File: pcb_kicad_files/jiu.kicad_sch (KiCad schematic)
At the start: 173 parts, among them J1 2x3 2.54mm pitch pin header, J2 TYPE-C-31-M-12, J3 1x5 2.54mm pitch pin header, J4 2x9 2.54mm pitch pin header, Q1 DTC123JKAT146, SW1 1U, SW10 1U, SW11 1U, SW12 1U, SW13 1U, SW14 1U, SW15 1U, SW16 2u, SW17 1.5U, SW18 1U, SW19 1U, SW2 1U, SW20 1U, SW21 1U, SW22 1U, SW23 1U, SW24 1U, SW25 1U, SW26 1U, SW27 1U, SW28 1U, SW29 1U, SW3 1U, SW30 1.5U, SW31 1U, SW32 1.75U, SW33 1U, SW34 1U, SW35 1U, SW36 1U, SW37 1U, SW38 1U, SW39 1U, SW4 1U, SW40 1U, SW41 1U, SW42 1U, SW43 1U, SW44 2.25U, SW45 1U, SW46 1.25U, SW47 2.25U, SW48 1U, SW49 1U, SW5 1U, SW50 1U, SW51 1U, SW52 1U, SW53 1U, SW54 1U, SW55 1U, SW56 1U, SW57 1U, SW58 1.75U, SW59 1U, SW6 1U, SW60 1U, SW61 1.5U, SW62 1U, SW63 1.5U, SW64 7U, SW65 1.5U, SW66 1U, SW67 1U, SW68 1U, SW69 1.25U, SW7 1U, SW70 1.25U, SW71 1.25U, SW72 6.25U, SW73 1.25U, SW74 K2-1187SQ-A4SW-06, SW8 1U, SW9 1U, U1 USBLC6-2SC6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

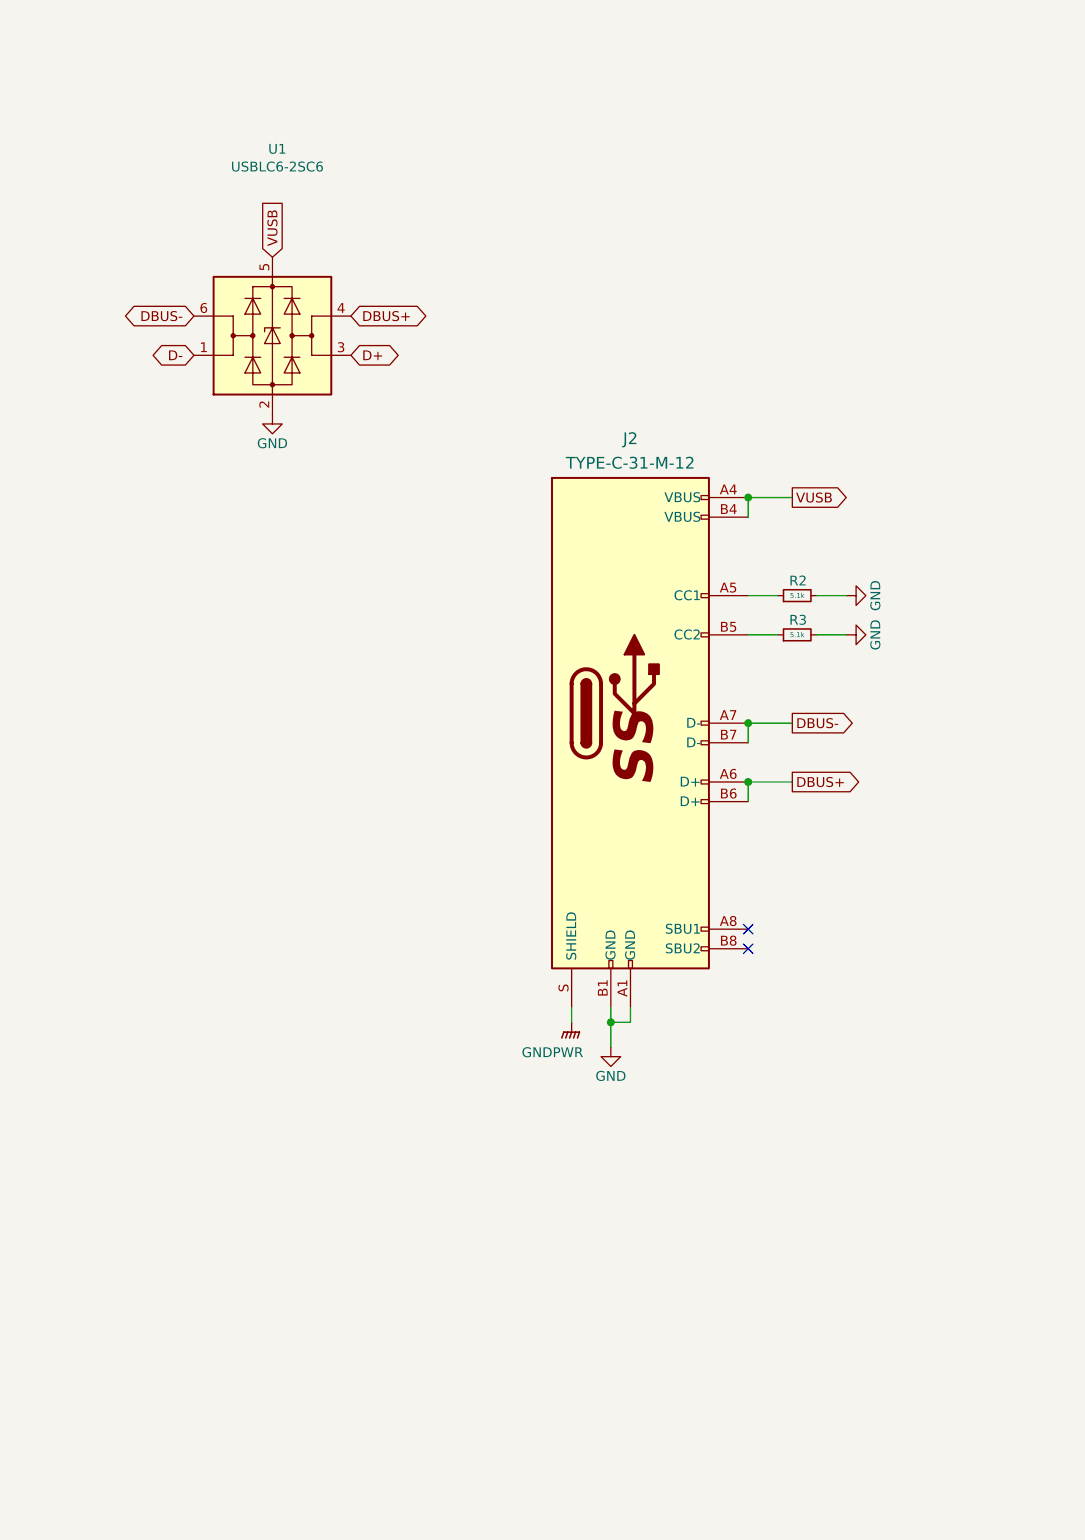
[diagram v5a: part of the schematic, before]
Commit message: Added ferrite bead to USB shield and ground
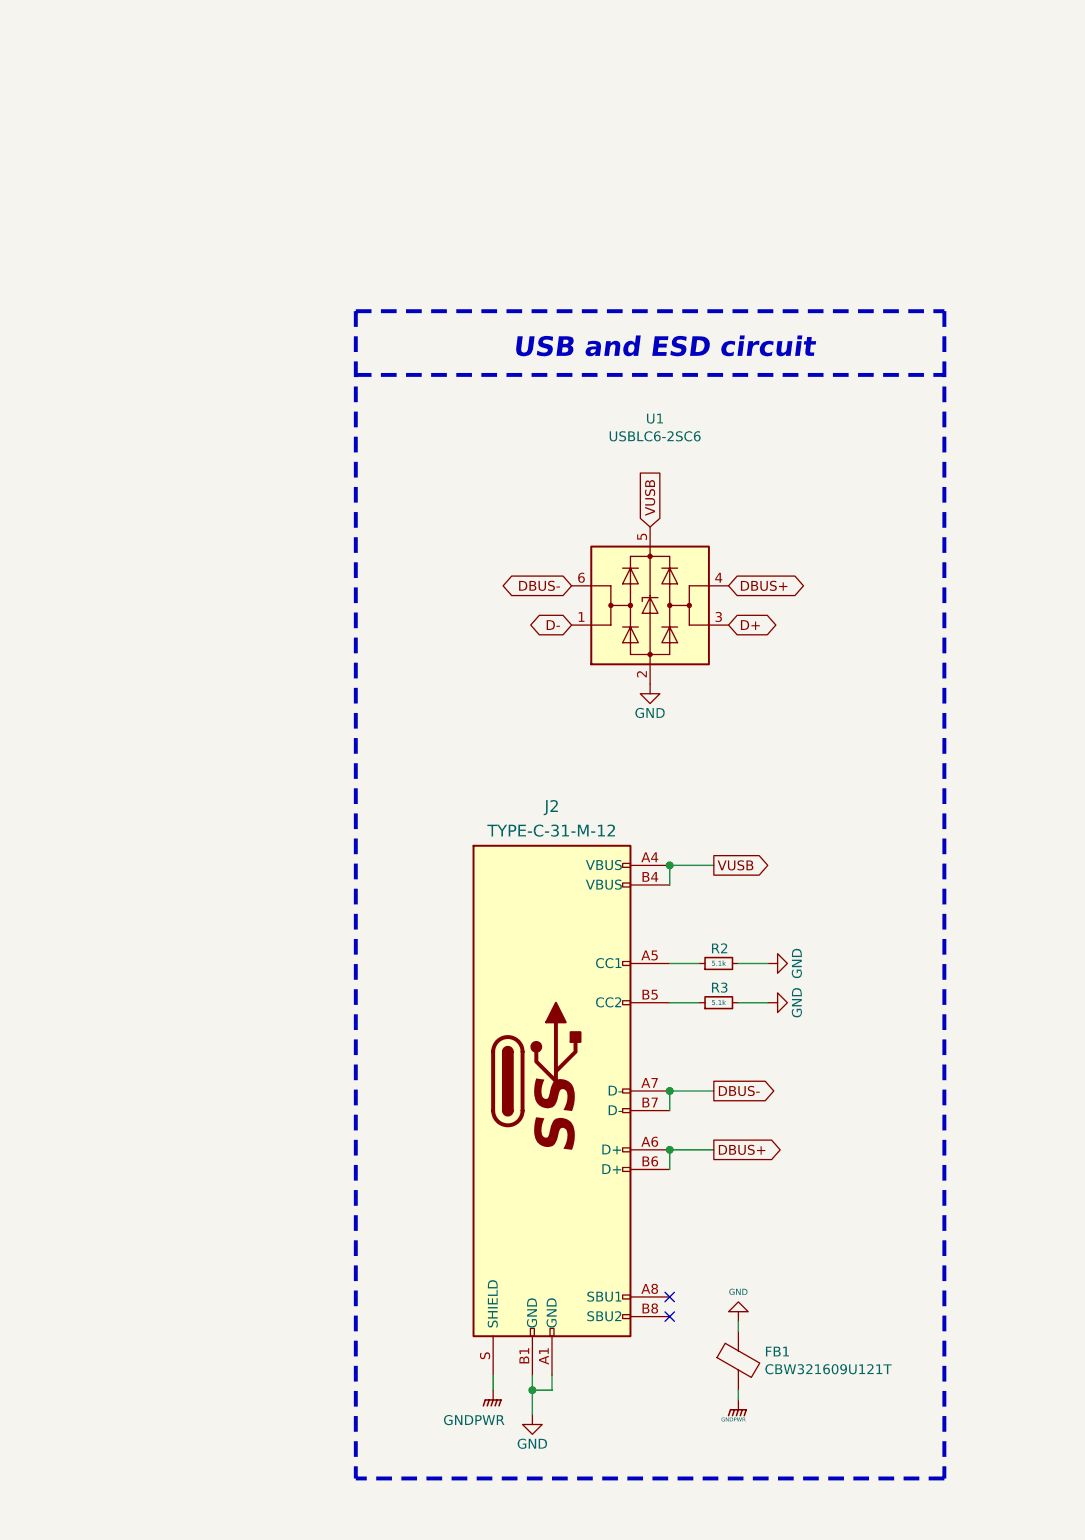
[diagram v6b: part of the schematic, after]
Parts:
- added FB1: CBW321609U121T, Inductor_SMD:L_1206_3216Metric, symbol Device:Ferrite_Bead
- D67: Package (none) -> SOD-123
- D68: Manufacturer (none) -> ROHM Semicon; Manufacturer Part Number (none) -> RB060M-60TR; Package (none) -> SOD-123; Specification (none) -> Power rectifier schottky diode
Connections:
- net GND: now also FB1.1
- net GNDPWR: now also FB1.2
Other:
- note added: "USB and ESD circuit"
- moved on the sheet: J2, R2, R3, U1

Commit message: Preparing for pre-release Alpha
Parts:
- C1, C4: Package (none) -> C0805; Specification (none) -> MLCC 10V
- C10, C9: Package (none) -> CT3216
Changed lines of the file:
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@@
+      (effects (font (size 1.27 1.27)) hide)
+    )
+    (property "Package" "CT3216" (id 4) (at 195.58 340.995 0)
       (effects (font (size 1.27 1.27)) hide)
     )
@@
       (effects (font (size 1.27 1.27)) hide)
     )
+    (property "Package" "CT3216" (id 4) (at 213.36 340.995 0)
+      (effects (font (size 1.27 1.27)) hide)
+    )
   )
   (symbol (lib_id "Device:C_Small") (at 203.835 261.62 180) (unit 1)
@@
     )
     (property "Datasheet" "~" (id 3) (at 203.835 261.62 0)
+      (effects (font (size 1.27 1.27)) hide)
+    )
+    (property "Package" "C0805" (id 4) (at 203.835 261.62 0)
+      (effects (font (size 1.27 1.27)) hide)
+    )
+    (property "Specification" "MLCC 10V" (id 4) (at 203.835 261.62 0)
       (effects (font (size 1.27 1.27)) hide)
     )
@@
       (effects (font (size 1.27 1.27)) hide)
     )
+    (property "Package" "C0805" (id 4) (at 209.55 285.75 0)
+      (effects (font (size 1.27 1.27)) hide)
+    )
+    (property "Specification" "MLCC 10V" (id 4) (at 209.55 285.75 0)
+      (effects (font (size 1.27 1.27)) hide)
+    )

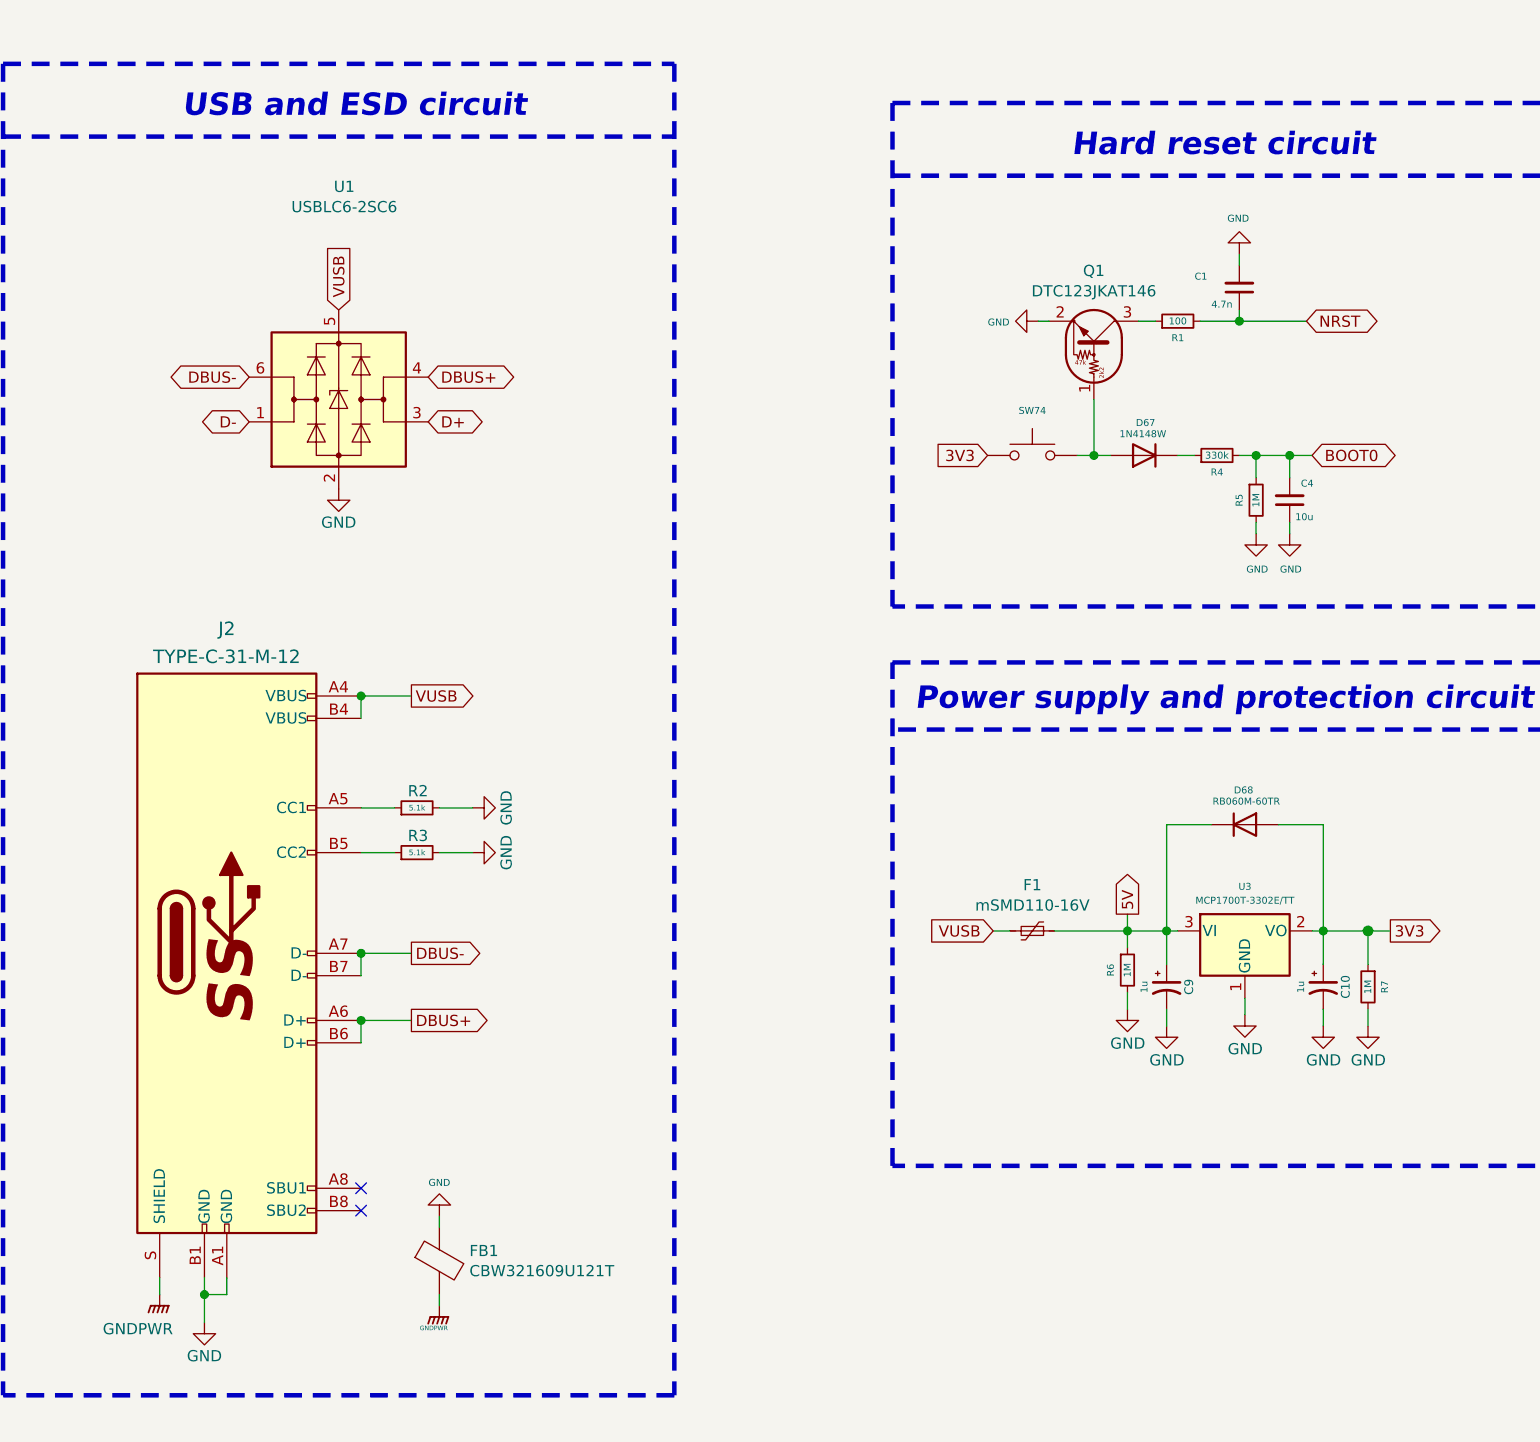
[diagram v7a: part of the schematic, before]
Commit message: Change components and ratings to JLC assembly
- Components were swapped for units that could be soldered in JLCPCB's assembly using the most basic components possible
- All resistors were changed to 0805
- Reset button was removed and instead reset contacts were exposed; resetting PCB will require shorting the contacts with pliers
- Reset circuitry was changed for a 2N7002 MOSFET variant since JLC has no digital transistors in their roster of basic parts
- USB connector and MCU could not be changed as there are no equivalent substitutes in the basic parts but they are completely essential
- USB ESD device was changed for a four-way variant that is a JLC basic part; USB data traces were changed accordingly
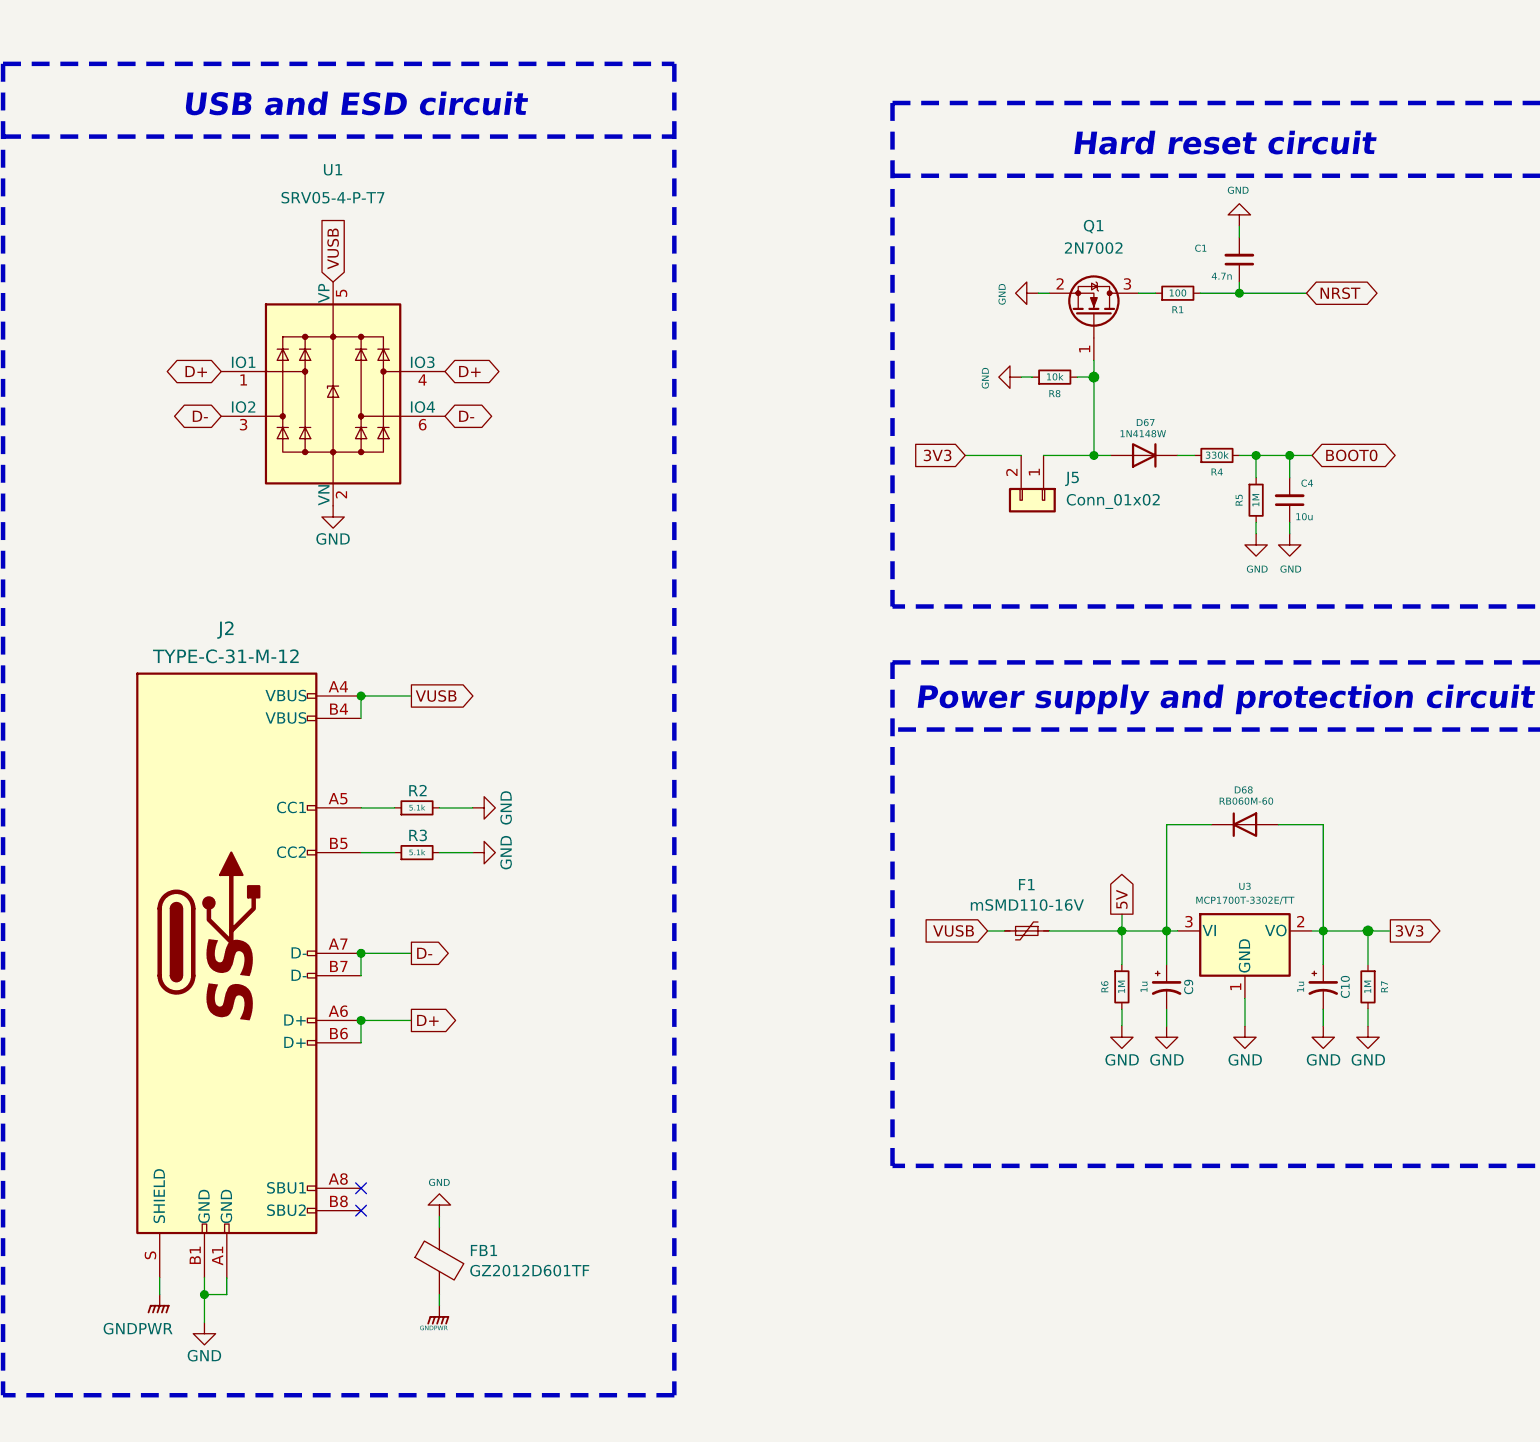
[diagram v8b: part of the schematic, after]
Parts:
- removed Q1: DTC123JKAT146, Package_TO_SOT_SMD:SOT-23, symbol Transistor_BJT:DTC123J
- removed SW74: K2-1187SQ-A4SW-06, acheron_Hardware:K2-1187SQ-A4SW-06, symbol Switch:SW_Push
- removed U1: USBLC6-2SC6, acheron_Components:SOT-23-6, symbol Power_Protection:USBLC6-2SC6
- added J5: Conn_01x02, acheron_Hardware:THT_reset_contacts, symbol Connector_Generic:Conn_01x02
- added Q1: 2N7002, Package_TO_SOT_SMD:SOT-23, symbol Transistor_FET:2N7002
- added R8: 10k, Resistor_SMD:R_0805_2012Metric, symbol Device:R_Small
- added U1: SRV05-4-P-T7, acheron_Components:SOT-23-6, symbol Power_Protection:SRV05-4
- D68: value RB060M-60TR -> RB060M-60; LCSC Part Number (none) -> C115330; Manufacturer ROHM Semicon -> Shikues; Manufacturer Part Number RB060M-60TR -> RB060M-60; Package SOD-123 -> SOD-123F
- FB1: value CBW321609U121T -> GZ2012D601TF; footprint Inductor_SMD:L_1206_3216Metric -> Inductor_SMD:L_0805_2012Metric; LCSC Part Number C139197 -> C1017; Package L1206 -> L0805; Specification 120Ω @ 100MHz 3A 1 70mΩ ferrite bead -> 600Ω @ 100MHz 500mA 300mΩ 0805 ferrite bead
- R1, R2, R3, R4, R5, R6, R7: footprint acheron_Components:R_SMD_1206 -> Resistor_SMD:R_0805_2012Metric; Package R1206 -> R0805
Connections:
- net DBUS+ is gone; now on net D+: J2.A6 (D+), J2.B6 (D+)
- net DBUS- is gone; now on net D-: J2.A7 (D-), J2.B7 (D-)
- net 3V3: now also J5.2 (Pin_2)
- net D+: now also U1.1 (IO1), U1.4 (IO3)
- net D-: now also U1.3 (IO2), U1.6 (IO4)
- net GND: now also Q1.2 (S), R8.1, U1.2 (VN)
- net VUSB: now also U1.5 (VP)
- net at D67.2 (A): now also J5.1 (Pin_1), Q1.1 (G), R8.2
- net at R1.1: now also Q1.3 (D)
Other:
- moved on the sheet: C1, F1, R1, R6
